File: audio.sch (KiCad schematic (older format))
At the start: 25 parts, among them J1301 CTIA / AHJ, U1301 SGTL5000

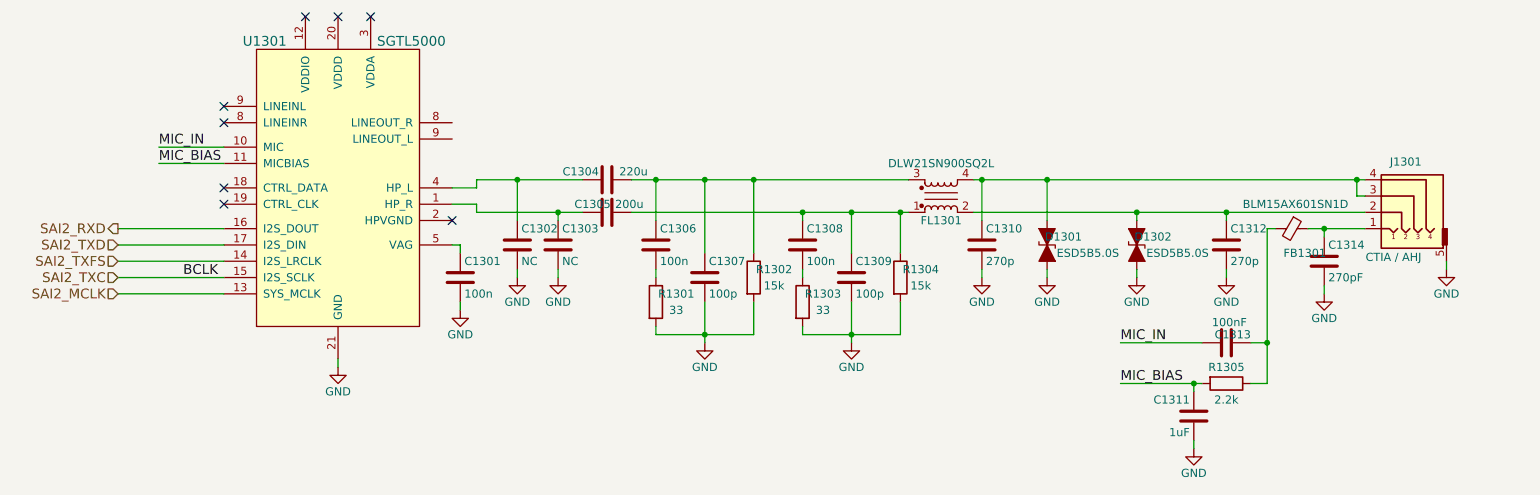
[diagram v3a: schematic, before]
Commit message: Move reference designators in the schematic so that they are legible
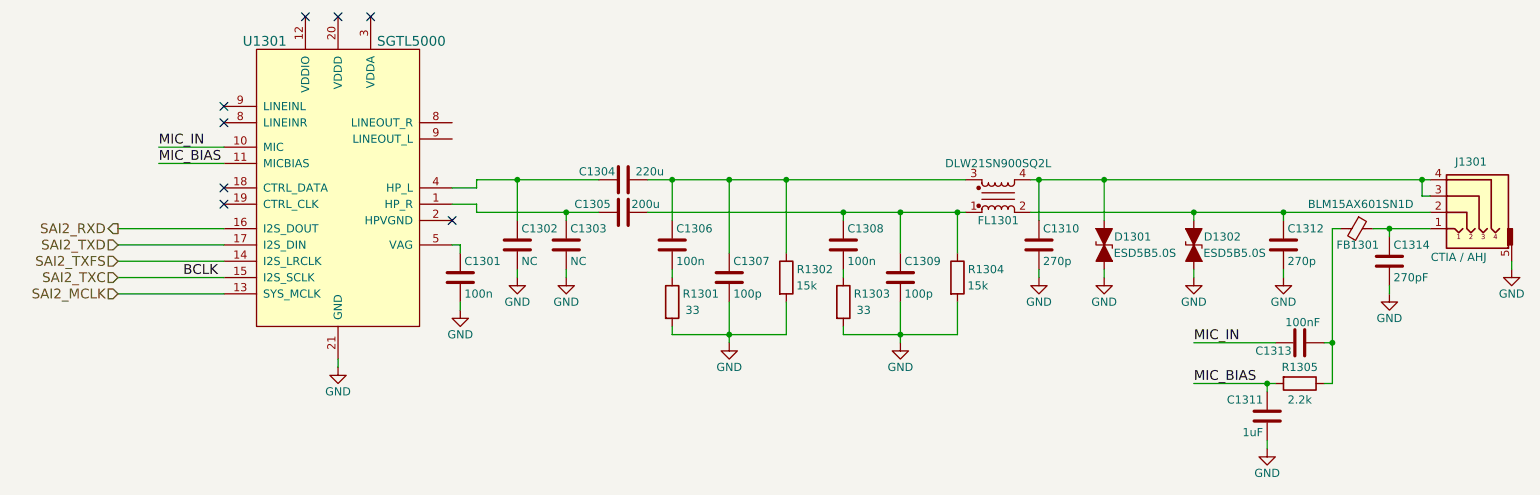
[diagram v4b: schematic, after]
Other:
- moved on the sheet: C1303, C1304, C1305, C1306, C1307, C1308, C1309, C1310, C1311, C1312, C1313, C1314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

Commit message: Include reverse polarity protection circuit along with a simulation showing its effectiveness
Protecting VBAT from when board is sinking current via USB C. Protects against reverse polarity at the DC jack.

In EmCraft's instance VBUS should only be 5V when sinking current but they must protect against the condition when VBUS>12V and DC_IN=12V. This may need testing.
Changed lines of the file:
@@
 Sheet 13 14
 Title "Audio"
-Date "2018-04-16"
+Date "2018-04-18"
 Rev "v0.1.0"
 Comp "Purism SPC"
@@
 $EndComp
 $Comp
-L GND #PWR0159
+L GND #PWR0160
 U 1 1 5ABE80CA
 P 3050 4450
-F 0 "#PWR0159" H 3050 4200 50  0001 C CNN
+F 0 "#PWR0160" H 3050 4200 50  0001 C CNN
 F 1 "GND" H 3050 4300 50  0000 C CNN
 F 2 "" H 3050 4450 50  0001 C CNN
@@
 	3900 3350 3900 3300
 Wire Wire Line
-	3900 3300 4150 3300
-Wire Wire Line
-	4150 3300 4650 3300
+	3900 3300 4650 3300
 Wire Wire Line
 	3750 3450 3900 3450
@@
 	3900 3450 3900 3500
 Wire Wire Line
-	3900 3500 4450 3500
-Wire Wire Line
-	4450 3500 4650 3500
+	3900 3500 4650 3500
 $Comp
 L C C1302
@@
 $EndComp
 $Comp
-L GND #PWR0160
+L GND #PWR0161
 U 1 1 5ABEF777
 P 4450 3900
-F 0 "#PWR0160" H 4450 3650 50  0001 C CNN
+F 0 "#PWR0161" H 4450 3650 50  0001 C CNN
 F 1 "GND" H 4450 3750 50  0000 C CNN
 F 2 "" H 4450 3900 50  0001 C CNN
@@
 $EndComp
 $Comp
-L GND #PWR0161
+L GND #PWR0162
 U 1 1 5ABEF798
 P 4150 3900
-F 0 "#PWR0161" H 4150 3650 50  0001 C CNN
+F 0 "#PWR0162" H 4150 3650 50  0001 C CNN
 F 1 "GND" H 4150 3750 50  0000 C CNN
 F 2 "" H 4150 3900 50  0001 C CNN
@@
 $EndComp
 Wire Wire Line
-	4950 3500 6150 3500
-Wire Wire Line
-	6150 3500 6500 3500
-Wire Wire Line
-	6500 3500 6850 3500
-Wire Wire Line
-	6850 3500 6900 3500
-Wire Wire Line
-	4950 3300 5100 3300
-Wire Wire Line
-	5100 3300 5450 3300
-Wire Wire Line
-	5450 3300 5800 3300
-Wire Wire Line
-	5800 3300 6900 3300
+	4950 3500 6900 3500
+Wire Wire Line
+	4950 3300 6900 3300
 Wire Wire Line
 	5100 3850 5100 3900
 $Comp
-L GND #PWR0162
+L GND #PWR0163
 U 1 1 5ABF0047
 P 5450 4300
-F 0 "#PWR0162" H 5450 4050 50  0001 C CNN
+F 0 "#PWR0163" H 5450 4050 50  0001 C CNN
 F 1 "GND" H 5450 4150 50  0000 C CNN
 F 2 "" H 5450 4300 50  0001 C CNN
@@
 $EndComp
 Wire Wire Line
-	7300 3300 7350 3300
-Wire Wire Line
-	7350 3300 7750 3300
-Wire Wire Line
-	7750 3300 9700 3300
-Wire Wire Line
-	9700 3300 9750 3300
+	7300 3300 9750 3300
 Wire Wire Line
 	7350 3300 7350 3550
 Wire Wire Line
-	7300 3500 8300 3500
-Wire Wire Line
-	8300 3500 8850 3500
-Wire Wire Line
-	8850 3500 9750 3500
+	7300 3500 9750 3500
 Wire Wire Line
 	8850 3500 8850 3550
 $Comp
-L GND #PWR0163
+L GND #PWR0164
 U 1 1 5ABF2BDF
 P 8850 3900
-F 0 "#PWR0163" H 8850 3650 50  0001 C CNN
+F 0 "#PWR0164" H 8850 3650 50  0001 C CNN
 F 1 "GND" H 8850 3750 50  0000 C CNN
 F 2 "" H 8850 3900 50  0001 C CNN
@@
 	8850 3900 8850 3850
 $Comp
-L GND #PWR0164
+L GND #PWR0165
 U 1 1 5ABF2C32
 P 7350 3900
-F 0 "#PWR0164" H 7350 3650 50  0001 C CNN
+F 0 "#PWR0165" H 7350 3650 50  0001 C CNN
 F 1 "GND" H 7350 3750 50  0000 C CNN
 F 2 "" H 7350 3900 50  0001 C CNN
@@
 $EndComp
 Wire Wire Line
-	5100 4250 5450 4250
-Wire Wire Line
-	5450 4250 5800 4250
+	5100 4250 5800 4250
 Wire Wire Line
 	5800 4250 5800 4050
 Wire Wire Line
-	5450 4050 5450 4250
-Wire Wire Line
-	5450 4250 5450 4300
+	5450 4050 5450 4300
 Connection ~ 5450 4250
 Wire Wire Line
@@
 	6150 3850 6150 3900
 $Comp
-L GND #PWR0165
+L GND #PWR0166
 U 1 1 5ABF53B5
 P 6500 4300
-F 0 "#PWR0165" H 6500 4050 50  0001 C CNN
+F 0 "#PWR0166" H 6500 4050 50  0001 C CNN
 F 1 "GND" H 6500 4150 50  0000 C CNN
 F 2 "" H 6500 4300 50  0001 C CNN
@@
 $EndComp
 Wire Wire Line
-	6150 4250 6500 4250
-Wire Wire Line
-	6500 4250 6850 4250
+	6150 4250 6850 4250
 Wire Wire Line
 	6850 4250 6850 4050
 Wire Wire Line
-	6500 4050 6500 4250
-Wire Wire Line
-	6500 4250 6500 4300
+	6500 4050 6500 4300
 Connection ~ 6500 4250
 Wire Wire Line
@@
 $EndComp
 $Comp
-L GND #PWR0166
+L GND #PWR0167
 U 1 1 5ABF847B
 P 7750 3900
-F 0 "#PWR0166" H 7750 3650 50  0001 C CNN
+F 0 "#PWR0167" H 7750 3650 50  0001 C CNN
 F 1 "GND" H 7750 3750 50  0000 C CNN
 F 2 "" H 7750 3900 50  0001 C CNN
@@
 	8300 3500 8300 3550
 $Comp
-L GND #PWR0167
+L GND #PWR0168
 U 1 1 5ABF8745
 P 8300 3900
-F 0 "#PWR0167" H 8300 3650 50  0001 C CNN
+F 0 "#PWR0168" H 8300 3650 50  0001 C CNN
 F 1 "GND" H 8300 3750 50  0000 C CNN
 F 2 "" H 8300 3900 50  0001 C CNN
@@
 Connection ~ 9700 3300
 $Comp
-L GND #PWR0168
+L GND #PWR0169
 U 1 1 5ABFAC4D
 P 10250 3850
-F 0 "#PWR0168" H 10250 3600 50  0001 C CNN
+F 0 "#PWR0169" H 10250 3600 50  0001 C CNN
 F 1 "GND" H 10250 3700 50  0000 C CNN
 F 2 "" H 10250 3850 50  0001 C CNN
@@
 $EndComp
 $Comp
-L GND #PWR0169
+L GND #PWR0170
 U 1 1 5ABFCB56
 P 3800 4100
-F 0 "#PWR0169" H 3800 3850 50  0001 C CNN
+F 0 "#PWR0170" H 3800 3850 50  0001 C CNN
 F 1 "GND" H 3800 3950 50  0000 C CNN
 F 2 "" H 3800 4100 50  0001 C CNN
@@
 $EndComp
 $Comp
-L GND #PWR0170
+L GND #PWR0171
 U 1 1 5AC7A8FB
 P 9500 4000
-F 0 "#PWR0170" H 9500 3750 50  0001 C CNN
+F 0 "#PWR0171" H 9500 3750 50  0001 C CNN
 F 1 "GND" H 9500 3850 50  0000 C CNN
 F 2 "" H 9500 4000 50  0001 C CNN
@@
 Connection ~ 9500 3600
 Wire Wire Line
-	9400 3600 9500 3600
-Wire Wire Line
-	9500 3600 9750 3600
+	9400 3600 9750 3600
 $Comp
 L R R1305
@@
 $EndComp
 Wire Wire Line
-	9150 3600 9150 4300
-Wire Wire Line
-	9150 4300 9150 4550
+	9150 3600 9150 4550
 Wire Wire Line
 	9150 3600 9200 3600
@@
 	9150 4550 9100 4550
 Wire Wire Line
-	8300 4550 8750 4550
-Wire Wire Line
-	8750 4550 8800 4550
+	8300 4550 8800 4550
 Wire Wire Line
 	8750 4600 8750 4550
 Connection ~ 8750 4550
 $Comp
-L GND #PWR0171
+L GND #PWR0172
 U 1 1 5AC7C780
 P 8750 4950
-F 0 "#PWR0171" H 8750 4700 50  0001 C CNN
+F 0 "#PWR0172" H 8750 4700 50  0001 C CNN
 F 1 "GND" H 8750 4800 50  0000 C CNN
 F 2 "" H 8750 4950 50  0001 C CNN

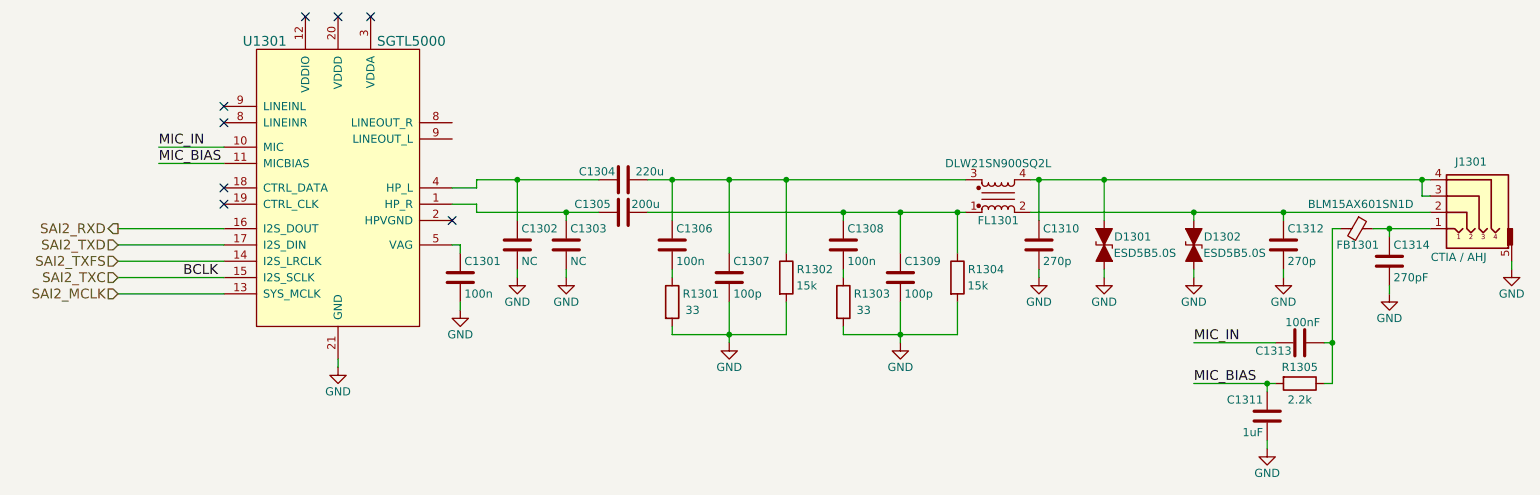
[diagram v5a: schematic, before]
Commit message: Stick the WWAM M.2 sheet above/before the audio sheet
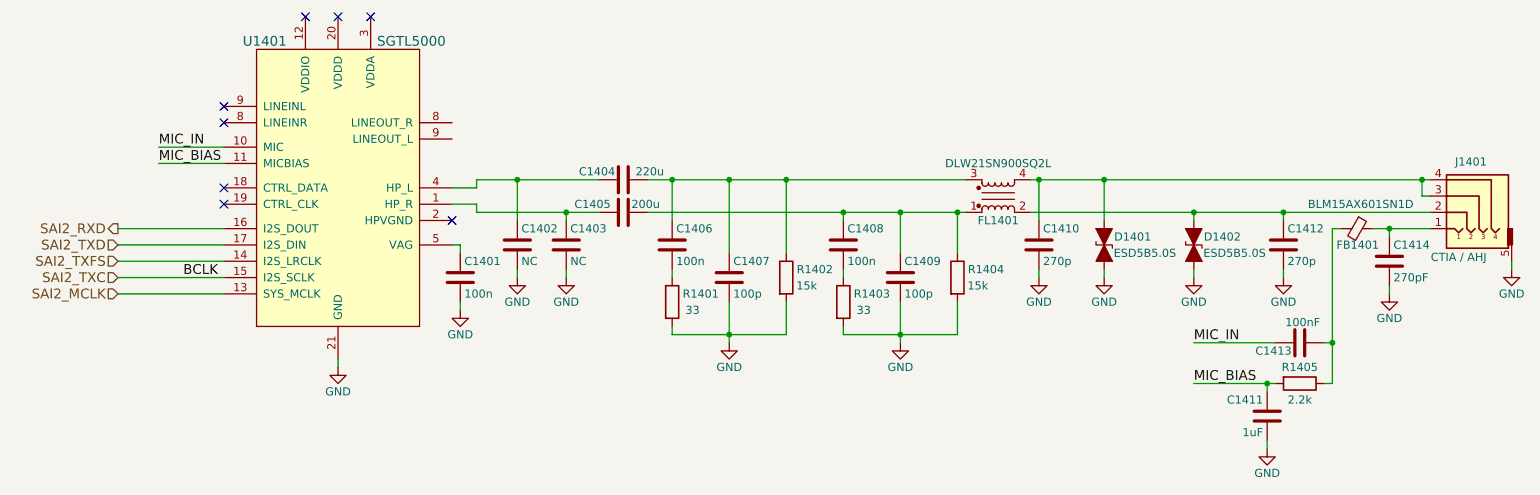
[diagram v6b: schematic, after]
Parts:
- renumbered C1301 to C1401, C1302 to C1402, C1303 to C1403, C1304 to C1404, C1305 to C1405, C1306 to C1406, C1307 to C1407, C1308 to C1408, C1309 to C1409, C1310 to C1410, C1311 to C1411, C1312 to C1412, C1313 to C1413, C1314 to C1414, D1301 to D1401, D1302 to D1402, FB1301 to FB1401, FL1301 to FL1401, J1301 to J1401, R1301 to R1401, R1302 to R1402, R1303 to R1403, R1304 to R1404, R1305 to R1405, U1301 to U1401
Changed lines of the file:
@@
 $Descr A4 11693 8268
 encoding utf-8
-Sheet 13 14
+Sheet 14 14
 Title "Audio"
 Date "2018-04-18"
@@
 $EndDescr
 $Comp
-L SGTL5000 U1301
+L SGTL5000 U1401
 U 1 1 5ABE7D8D
 P 3050 3350
-F 0 "U1301" H 2600 4250 60  0000 C CNN
+F 0 "U1401" H 2600 4250 60  0000 C CNN
 F 1 "SGTL5000" H 3500 4250 60  0000 C CNN
 F 2 "" H 3050 3400 60  0000 C CNN
@@
 $EndComp
 $Comp
-L GND #PWR0160
+L GND #PWR0191
 U 1 1 5ABE80CA
 P 3050 4450
-F 0 "#PWR0160" H 3050 4200 50  0001 C CNN
+F 0 "#PWR0191" H 3050 4200 50  0001 C CNN
 F 1 "GND" H 3050 4300 50  0000 C CNN
 F 2 "" H 3050 4450 50  0001 C CNN
@@
 	1700 3900 2350 3900
 $Comp
-L C C1304
+L C C1404
 U 1 1 5ABEEF4C
 P 4800 3300
-F 0 "C1304" V 4850 3350 50  0000 L CNN
+F 0 "C1404" V 4850 3350 50  0000 L CNN
 F 1 "220u" V 4850 3050 50  0000 L CNN
 F 2 "" H 4838 3150 50  0001 C CNN
@@
 $EndComp
 $Comp
-L C C1305
+L C C1405
 U 1 1 5ABEEF73
 P 4800 3500
-F 0 "C1305" V 4850 3200 50  0000 L CNN
+F 0 "C1405" V 4850 3200 50  0000 L CNN
 F 1 "200u" V 4850 3550 50  0000 L CNN
 F 2 "" H 4838 3350 50  0001 C CNN
@@
 	3900 3500 4650 3500
 $Comp
-L C C1302
+L C C1402
 U 1 1 5ABEF358
 P 4150 3700
-F 0 "C1302" H 4175 3800 50  0000 L CNN
+F 0 "C1402" H 4175 3800 50  0000 L CNN
 F 1 "NC" H 4175 3600 50  0000 L CNN
 F 2 "" H 4188 3550 50  0001 C CNN
@@
 $EndComp
 $Comp
-L C C1303
+L C C1403
 U 1 1 5ABEF388
 P 4450 3700
-F 0 "C1303" H 4475 3800 50  0000 L CNN
+F 0 "C1403" H 4475 3800 50  0000 L CNN
 F 1 "NC" H 4475 3600 50  0000 L CNN
 F 2 "" H 4488 3550 50  0001 C CNN
@@
 $EndComp
 $Comp
-L GND #PWR0161
+L GND #PWR0192
 U 1 1 5ABEF777
 P 4450 3900
-F 0 "#PWR0161" H 4450 3650 50  0001 C CNN
+F 0 "#PWR0192" H 4450 3650 50  0001 C CNN
 F 1 "GND" H 4450 3750 50  0000 C CNN
 F 2 "" H 4450 3900 50  0001 C CNN
@@
 $EndComp
 $Comp
-L GND #PWR0162
+L GND #PWR0193
 U 1 1 5ABEF798
 P 4150 3900
-F 0 "#PWR0162" H 4150 3650 50  0001 C CNN
+F 0 "#PWR0193" H 4150 3650 50  0001 C CNN
 F 1 "GND" H 4150 3750 50  0000 C CNN
 F 2 "" H 4150 3900 50  0001 C CNN
@@
 	4150 3850 4150 3900
 $Comp
-L R R1301
+L R R1401
 U 1 1 5ABEFC7B
 P 5100 4050
-F 0 "R1301" H 5275 4100 50  0000 C CNN
+F 0 "R1401" H 5275 4100 50  0000 C CNN
 F 1 "33" H 5225 4000 50  0000 C CNN
 F 2 "" V 5030 4050 50  0001 C CNN
@@
 	5100 3850 5100 3900
 $Comp
-L GND #PWR0163
+L GND #PWR0194
 U 1 1 5ABF0047
 P 5450 4300
-F 0 "#PWR0163" H 5450 4050 50  0001 C CNN
+F 0 "#PWR0194" H 5450 4050 50  0001 C CNN
 F 1 "GND" H 5450 4150 50  0000 C CNN
 F 2 "" H 5450 4300 50  0001 C CNN
@@
 	5100 4200 5100 4250
 $Comp
-L EMI_Filter_CommonMode FL1301
+L EMI_Filter_CommonMode FL1401
 U 1 1 5ABF2412
 P 7100 3400
-F 0 "FL1301" H 7100 3550 50  0000 C CNN
+F 0 "FL1401" H 7100 3550 50  0000 C CNN
 F 1 "DLW21SN900SQ2L" H 7100 3200 50  0000 C CNN
 F 2 "" V 7100 3440 50  0000 C CNN
@@
 $EndComp
 $Comp
-L C C1312
+L C C1412
 U 1 1 5ABF2943
 P 8850 3700
-F 0 "C1312" H 8875 3800 50  0000 L CNN
+F 0 "C1412" H 8875 3800 50  0000 L CNN
 F 1 "270p" H 8875 3600 50  0000 L CNN
 F 2 "" H 8888 3550 50  0001 C CNN
@@
 $EndComp
 $Comp
-L C C1310
+L C C1410
 U 1 1 5ABF2987
 P 7350 3700
-F 0 "C1310" H 7375 3800 50  0000 L CNN
+F 0 "C1410" H 7375 3800 50  0000 L CNN
 F 1 "270p" H 7375 3600 50  0000 L CNN
 F 2 "" H 7388 3550 50  0001 C CNN
@@
 	8850 3500 8850 3550
 $Comp
-L GND #PWR0164
+L GND #PWR0195
 U 1 1 5ABF2BDF
 P 8850 3900
-F 0 "#PWR0164" H 8850 3650 50  0001 C CNN
+F 0 "#PWR0195" H 8850 3650 50  0001 C CNN
 F 1 "GND" H 8850 3750 50  0000 C CNN
 F 2 "" H 8850 3900 50  0001 C CNN
@@
 	8850 3900 8850 3850
 $Comp
-L GND #PWR0165
+L GND #PWR0196
 U 1 1 5ABF2C32
 P 7350 3900
-F 0 "#PWR0165" H 7350 3650 50  0001 C CNN
+F 0 "#PWR0196" H 7350 3650 50  0001 C CNN
 F 1 "GND" H 7350 3750 50  0000 C CNN
 F 2 "" H 7350 3900 50  0001 C CNN
@@
 Connection ~ 4150 3300
 $Comp
-L C C1306
+L C C1406
 U 1 1 5ABF4002
 P 5100 3700
-F 0 "C1306" H 5125 3800 50  0000 L CNN
+F 0 "C1406" H 5125 3800 50  0000 L CNN
 F 1 "100n" H 5125 3600 50  0000 L CNN
 F 2 "" H 5138 3550 50  0001 C CNN
@@
 $EndComp
 $Comp
-L C C1307
+L C C1407
 U 1 1 5ABF490A
 P 5450 3900
-F 0 "C1307" H 5475 4000 50  0000 L CNN
+F 0 "C1407" H 5475 4000 50  0000 L CNN
 F 1 "100p" H 5475 3800 50  0000 L CNN
 F 2 "" H 5488 3750 50  0001 C CNN
@@
 $EndComp
 $Comp
-L R R1302
+L R R1402
 U 1 1 5ABF49BF
 P 5800 3900
-F 0 "R1302" H 5975 3950 50  0000 C CNN
+F 0 "R1402" H 5975 3950 50  0000 C CNN
 F 1 "15k" H 5925 3850 50  0000 C CNN
 F 2 "" V 5730 3900 50  0001 C CNN
@@
 Connection ~ 5800 3300
 $Comp
-L R R1303
+L R R1403
 U 1 1 5ABF53AE
 P 6150 4050
-F 0 "R1303" H 6325 4100 50  0000 C CNN
+F 0 "R1403" H 6325 4100 50  0000 C CNN
 F 1 "33" H 6275 4000 50  0000 C CNN
 F 2 "" V 6080 4050 50  0001 C CNN
@@
 	6150 3850 6150 3900
 $Comp
-L GND #PWR0166
+L GND #PWR0197
 U 1 1 5ABF53B5
 P 6500 4300
-F 0 "#PWR0166" H 6500 4050 50  0001 C CNN
+F 0 "#PWR0197" H 6500 4050 50  0001 C CNN
 F 1 "GND" H 6500 4150 50  0000 C CNN
 F 2 "" H 6500 4300 50  0001 C CNN
@@
 	6150 4200 6150 4250
 $Comp
-L C C1308
+L C C1408
 U 1 1 5ABF53BC
 P 6150 3700
-F 0 "C1308" H 6175 3800 50  0000 L CNN
+F 0 "C1408" H 6175 3800 50  0000 L CNN
 F 1 "100n" H 6175 3600 50  0000 L CNN
 F 2 "" H 6188 3550 50  0001 C CNN
@@
 $EndComp
 $Comp
-L C C1309
+L C C1409
 U 1 1 5ABF53C2
 P 6500 3900
-F 0 "C1309" H 6525 4000 50  0000 L CNN
+F 0 "C1409" H 6525 4000 50  0000 L CNN
 F 1 "100p" H 6525 3800 50  0000 L CNN
 F 2 "" H 6538 3750 50  0001 C CNN
@@
 $EndComp
 $Comp
-L R R1304
+L R R1404
 U 1 1 5ABF53C8
 P 6850 3900
-F 0 "R1304" H 7025 3950 50  0000 C CNN
+F 0 "R1404" H 7025 3950 50  0000 C CNN
 F 1 "15k" H 6975 3850 50  0000 C CNN
 F 2 "" V 6780 3900 50  0001 C CNN
@@
 Connection ~ 6850 3500
 $Comp
-L D_TVS_ALT D1301
+L D_TVS_ALT D1401
 U 1 1 5ABF82C5
 P 7750 3700
-F 0 "D1301" V 7700 3875 50  0000 C CNN
+F 0 "D1401" V 7700 3875 50  0000 C CNN
 F 1 "ESD5B5.0S" V 7800 3950 50  0000 C CNN
 F 2 "" H 7750 3700 50  0001 C CNN
@@
 $EndComp
 $Comp
-L GND #PWR0167
+L GND #PWR0198
 U 1 1 5ABF847B
 P 7750 3900
-F 0 "#PWR0167" H 7750 3650 50  0001 C CNN
+F 0 "#PWR0198" H 7750 3650 50  0001 C CNN
 F 1 "GND" H 7750 3750 50  0000 C CNN
 F 2 "" H 7750 3900 50  0001 C CNN
@@
 	7750 3900 7750 3850
 $Comp
-L D_TVS_ALT D1302
+L D_TVS_ALT D1402
 U 1 1 5ABF8533
 P 8300 3700
-F 0 "D1302" V 8250 3875 50  0000 C CNN
+F 0 "D1402" V 8250 3875 50  0000 C CNN
 F 1 "ESD5B5.0S" V 8350 3950 50  0000 C CNN
 F 2 "" H 8300 3700 50  0001 C CNN
@@
 	8300 3500 8300 3550
 $Comp
-L GND #PWR0168
+L GND #PWR0199
 U 1 1 5ABF8745
 P 8300 3900
-F 0 "#PWR0168" H 8300 3650 50  0001 C CNN
+F 0 "#PWR0199" H 8300 3650 50  0001 C CNN
 F 1 "GND" H 8300 3750 50  0000 C CNN
 F 2 "" H 8300 3900 50  0001 C CNN
@@
 Connection ~ 8300 3500
 $Comp
-L Audio-Jack-5 J1301
+L Audio-Jack-5 J1401
 U 1 1 5ABF9919
 P 9950 3400
-F 0 "J1301" H 9900 3610 50  0000 C CNN
+F 0 "J1401" H 9900 3610 50  0000 C CNN
 F 1 "CTIA / AHJ" H 9975 3025 50  0000 C CNN
 F 2 "" H 10200 3500 50  0001 C CNN
@@
 Connection ~ 9700 3300
 $Comp
-L GND #PWR0169
+L GND #PWR0200
 U 1 1 5ABFAC4D
 P 10250 3850
-F 0 "#PWR0169" H 10250 3600 50  0001 C CNN
+F 0 "#PWR0200" H 10250 3600 50  0001 C CNN
 F 1 "GND" H 10250 3700 50  0000 C CNN
 F 2 "" H 10250 3850 50  0001 C CNN
@@
 MIC_IN
 $Comp
-L C C1301
+L C C1401
 U 1 1 5ABFC3EE
 P 3800 3900
-F 0 "C1301" H 3825 4000 50  0000 L CNN
+F 0 "C1401" H 3825 4000 50  0000 L CNN
 F 1 "100n" H 3825 3800 50  0000 L CNN
 F 2 "" H 3838 3750 50  0001 C CNN
@@
 $EndComp
 $Comp
-L GND #PWR0170
+L GND #PWR0201
 U 1 1 5ABFCB56
 P 3800 4100
-F 0 "#PWR0170" H 3800 3850 50  0001 C CNN
+F 0 "#PWR0201" H 3800 3850 50  0001 C CNN
 F 1 "GND" H 3800 3950 50  0000 C CNN
 F 2 "" H 3800 4100 50  0001 C CNN
@@
 NoConn ~ 3750 3550
 $Comp
-L C C1314
+L C C1414
 U 1 1 5AC79EEC
 P 9500 3800
-F 0 "C1314" H 9525 3900 50  0000 L CNN
+F 0 "C1414" H 9525 3900 50  0000 L CNN
 F 1 "270pF" H 9525 3700 50  0000 L CNN
 F 2 "" H 9538 3650 50  0001 C CNN
@@
 $EndComp
 $Comp
-L Ferrite_Bead_Small FB1301
+L Ferrite_Bead_Small FB1401
 U 1 1 5AC7A038
 P 9300 3600
-F 0 "FB1301" V 9400 3475 50  0000 L CNN
+F 0 "FB1401" V 9400 3475 50  0000 L CNN
 F 1 "BLM15AX601SN1D" V 9150 3300 50  0000 L CNN
 F 2 "" V 9230 3600 50  0001 C CNN
@@
 $EndComp
 $Comp
-L GND #PWR0171
+L GND #PWR0202
 U 1 1 5AC7A8FB
 P 9500 4000
-F 0 "#PWR0171" H 9500 3750 50  0001 C CNN
+F 0 "#PWR0202" H 9500 3750 50  0001 C CNN
 F 1 "GND" H 9500 3850 50  0000 C CNN
 F 2 "" H 9500 4000 50  0001 C CNN
@@
 	9400 3600 9750 3600
 $Comp
-L R R1305
+L R R1405
 U 1 1 5AC7B464
 P 8950 4550
-F 0 "R1305" V 8850 4550 50  0000 C CNN
+F 0 "R1405" V 8850 4550 50  0000 C CNN
 F 1 "2.2k" V 9050 4550 50  0000 C CNN
 F 2 "" V 8880 4550 50  0001 C CNN
@@
 	9150 3600 9200 3600
 $Comp
-L C C1313
+L C C1413
 U 1 1 5AC7B848
 P 8950 4300
-F 0 "C1313" V 8900 4350 50  0000 L CNN
+F 0 "C1413" V 8900 4350 50  0000 L CNN
 F 1 "100nF" V 9075 4175 50  0000 L CNN
 F 2 "" H 8988 4150 50  0001 C CNN
@@
 Connection ~ 9150 4300
 $Comp
-L C C1311
+L C C1411
 U 1 1 5AC7BC8A
 P 8750 4750
-F 0 "C1311" H 8775 4850 50  0000 L CNN
+F 0 "C1411" H 8775 4850 50  0000 L CNN
 F 1 "1uF" H 8775 4650 50  0000 L CNN
 F 2 "" H 8788 4600 50  0001 C CNN
@@
 Connection ~ 8750 4550
 $Comp
-L GND #PWR0172
+L GND #PWR0203
 U 1 1 5AC7C780
 P 8750 4950
-F 0 "#PWR0172" H 8750 4700 50  0001 C CNN
+F 0 "#PWR0203" H 8750 4700 50  0001 C CNN
 F 1 "GND" H 8750 4800 50  0000 C CNN
 F 2 "" H 8750 4950 50  0001 C CNN
